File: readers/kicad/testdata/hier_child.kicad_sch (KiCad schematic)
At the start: 2 parts

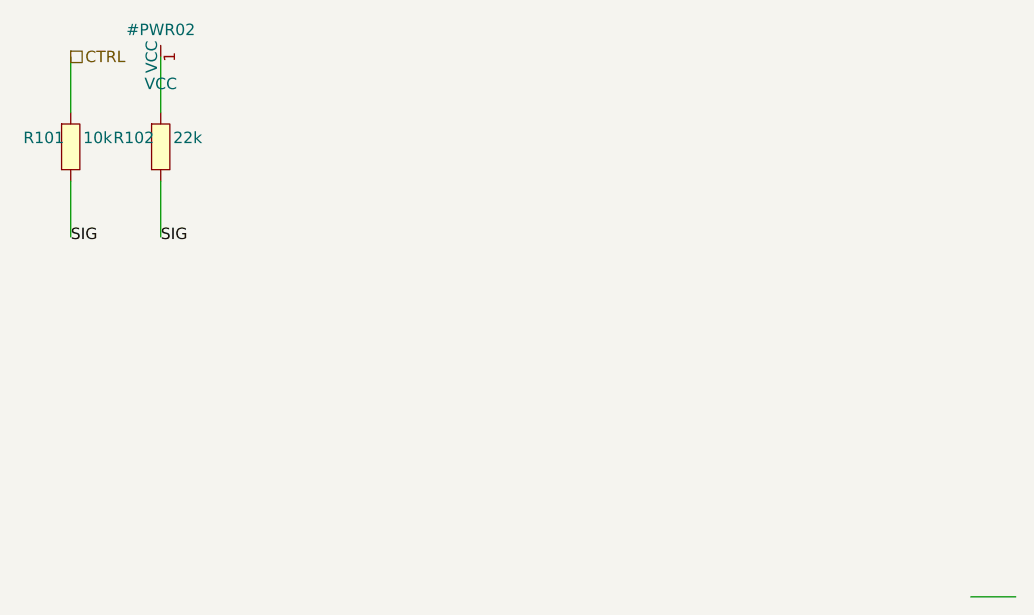
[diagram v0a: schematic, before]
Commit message: readers/kicad: report a schematic's unannotated parts
`unannotated_components` had one producer, so the rule that reads it was silent on every
format but EDIF. A KiCad schematic keeps its placeholder-designated symbols, which makes
it the layer that has to say they are unannotated: the parts are drawn and connected, so
by the time the IR reaches a rule they look like ordinary components with odd names.

The grouping helper moves from `readers/edif` to `internal/refdes` beside the predicate it
already used. A reader deriving its own is how the predicate stopped being single in the
first place, which is the shape of agni issue 311. Both KiCad schematic paths populate the
field, the single-file one and the hierarchical walk, which assembles its own
`InputDiagnostics`.

Also stops a double report. Two symbols reading `R?` were being recorded as a
`ref_des_collision` as well, which is an error-severity finding whose remedy is to rename
one of them. A placeholder is not a claimed designator, so those are not two parts
fighting over one name, and the collision detector now declines on one the same way the
pin-uniqueness index already does.

Out of scope: `ipc2581`, `geda` and `xschem` still record nothing.
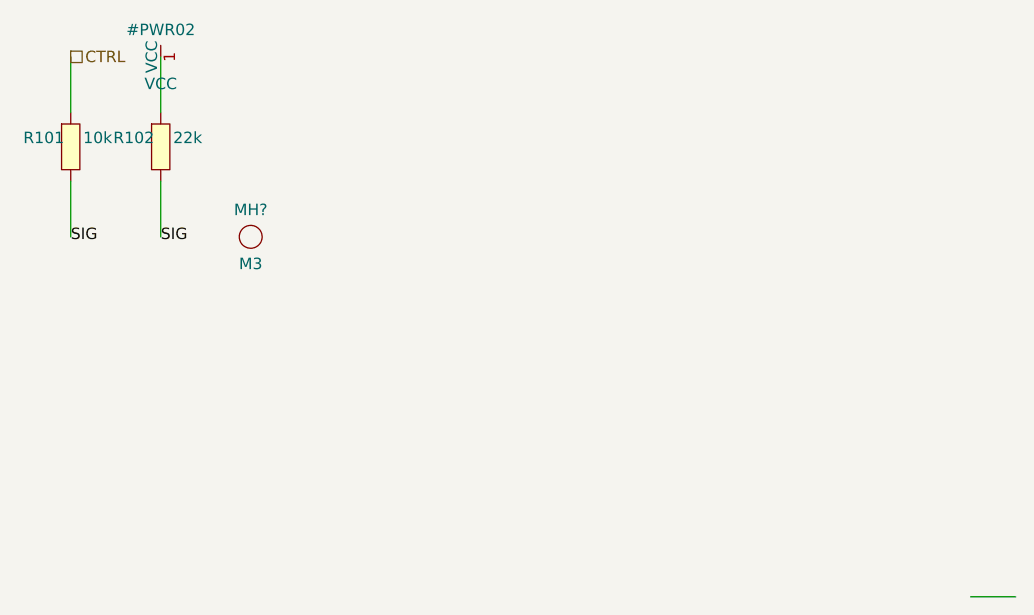
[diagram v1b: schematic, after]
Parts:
- added MH?: M3, symbol test:MH
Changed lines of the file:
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@@
 					(reference "R202")
 					(unit 1)))))
+	(symbol (lib_id "test:MH") (at 120 60 0) (unit 1) (uuid "childmh")
+		(property "Reference" "MH?"
+			(at 120 57 0)
+			(effects (font (size 1.27 1.27))))
+		(property "Value" "M3"
+			(at 120 63 0)
+			(effects (font (size 1.27 1.27)))))
 	(symbol (lib_id "power:VCC") (at 110 40 0) (unit 1) (uuid "childvcc")
 		(property "Reference" "#PWR02"
